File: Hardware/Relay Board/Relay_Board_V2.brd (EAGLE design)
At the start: 100.3 x 79.4 mm, 48 parts

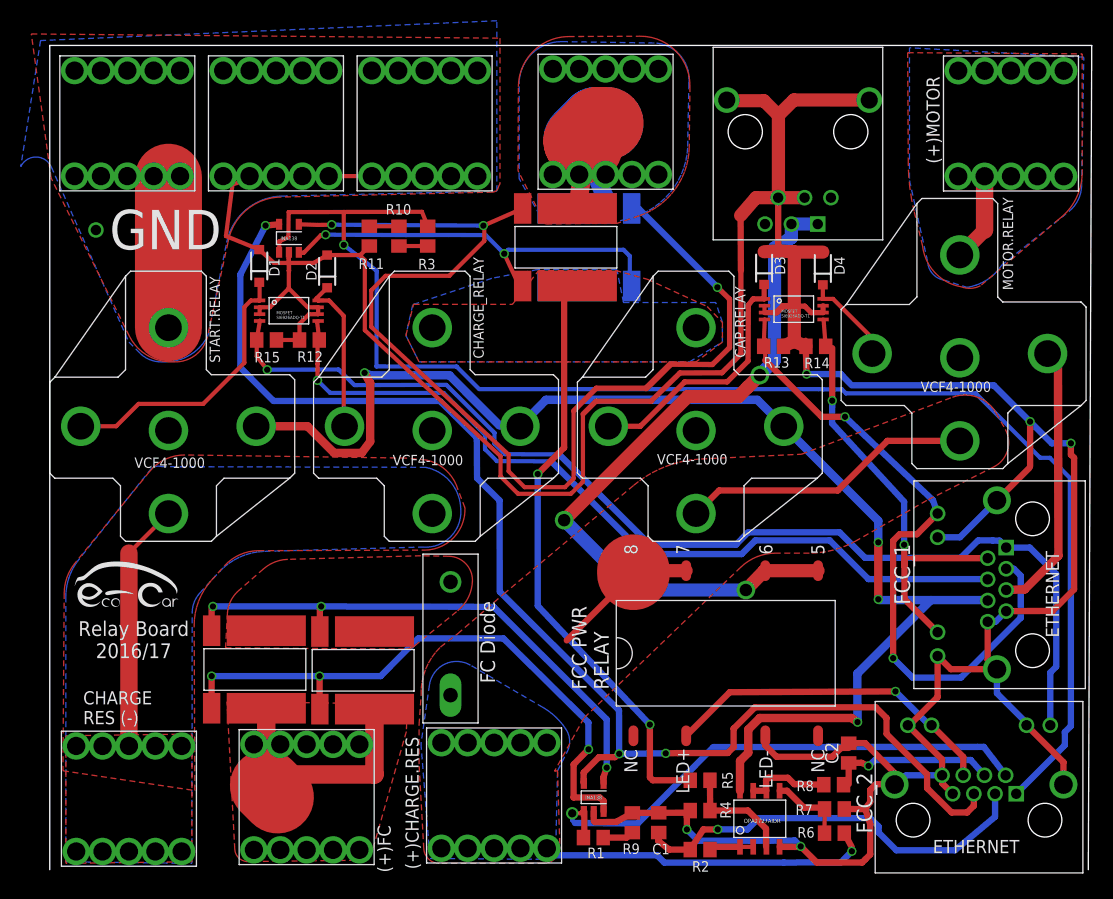
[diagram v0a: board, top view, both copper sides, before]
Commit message: added some example code and libraries
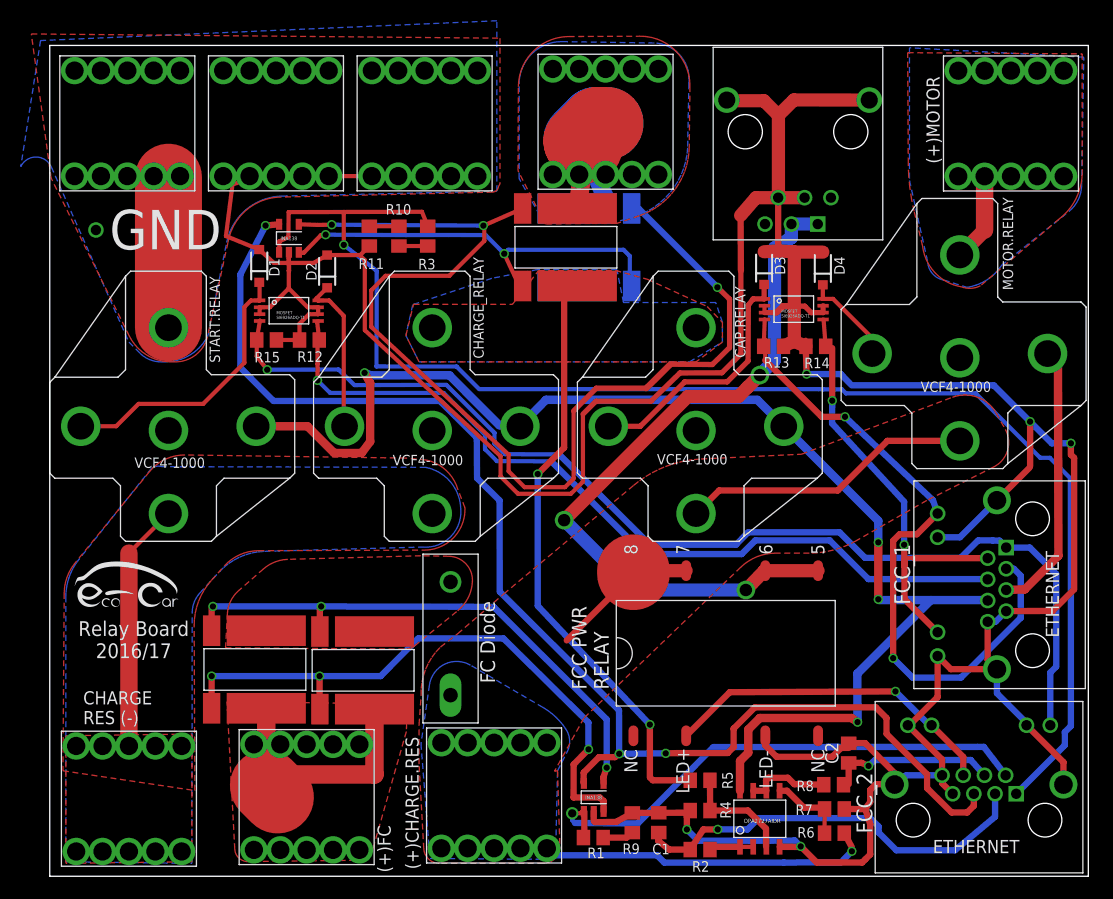
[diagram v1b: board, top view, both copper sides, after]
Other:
- board size 100.3 x 79.4 mm -> 100 x 80 mm
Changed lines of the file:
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@@
 <setting verticaltext="up"/>
 </settings>
-<grid distance="0.025" unitdist="inch" unit="inch" style="lines" multiple="1" display="no" altdistance="0.001" altunitdist="inch" altunit="inch"/>
+<grid distance="1" unitdist="mm" unit="mm" style="lines" multiple="1" display="no" altdistance="0.001" altunitdist="inch" altunit="inch"/>
 <layers>
 <layer number="1" name="Top" color="4" fill="1" visible="yes" active="yes"/>
@@
 <board>
 <plain>
-<wire x1="100" y1="0.635" x2="100.3302" y2="80" width="0" layer="20"/>
-<wire x1="100.3302" y1="80" x2="0" y2="80" width="0" layer="20"/>
-<wire x1="0" y1="80" x2="0" y2="0.635" width="0" layer="20"/>
 <text x="8.080375" y="22.7838" size="1.4224" layer="25" font="vector" ratio="18" align="center">Relay Board
 2016/17</text>
@@
 <text x="53.8226" y="17.9832" size="1.4224" layer="25" font="vector" ratio="18" rot="R90">FCC PWR
 RELAY</text>
+<wire x1="0" y1="0" x2="0" y2="80" width="0" layer="20"/>
+<wire x1="0" y1="80" x2="100" y2="80" width="0" layer="20"/>
+<wire x1="100" y1="80" x2="100" y2="0" width="0" layer="20"/>
+<wire x1="100" y1="0" x2="0" y2="0" width="0" layer="20"/>
 </plain>
 <attributes>
